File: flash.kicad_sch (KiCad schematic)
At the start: 16 parts, among them J5001 Tag-Connect_TC2050-IDC-NL_2x5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, J5002 Socket_SOP2-16_ACA-SPI-006-K0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, J5003 PinHeader_2x4_P2.54mm_Drill1.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, U5001 MT25QU01GBBB8_SOIC

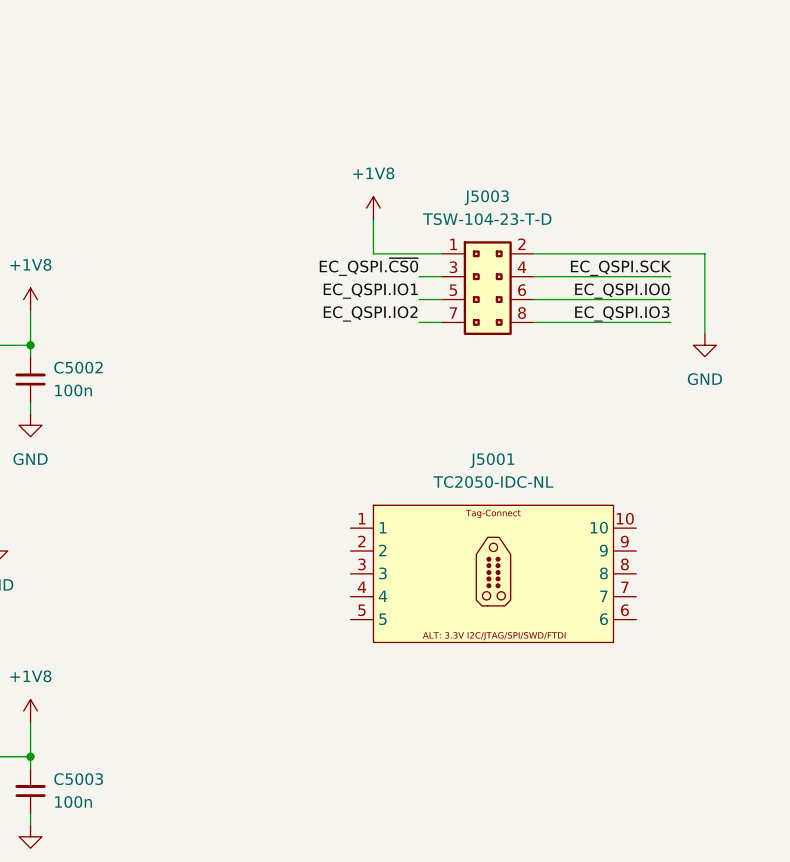
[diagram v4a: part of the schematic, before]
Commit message: [#103224] Add root schematic connections, add EMDRST button, add 1u decoupling capacitors, connect UART, add fiducials
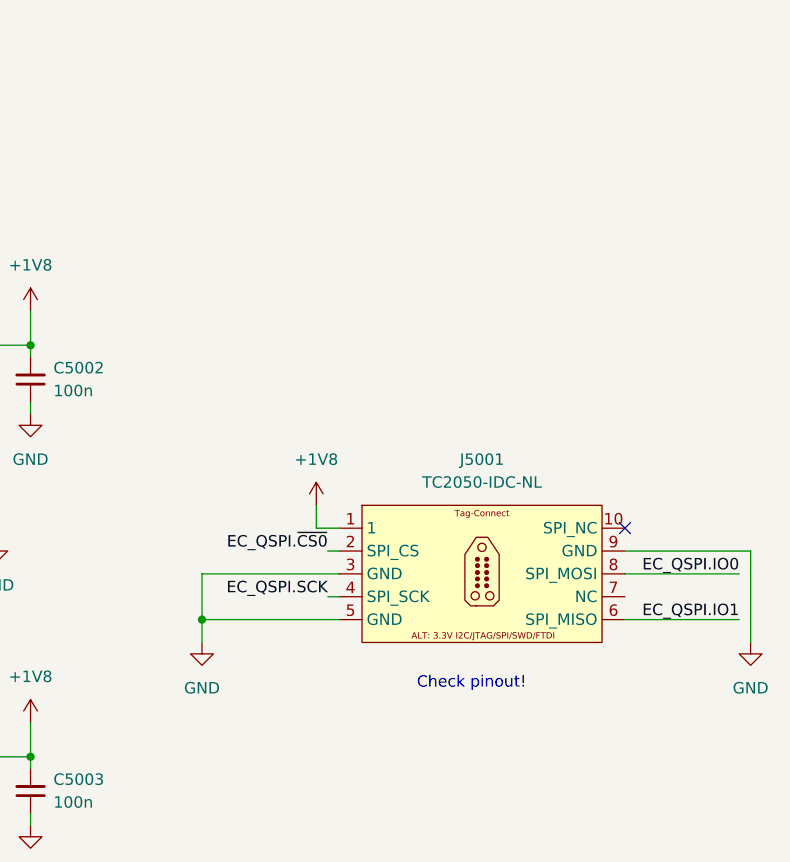
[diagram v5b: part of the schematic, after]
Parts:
- removed J5003: PinHeader_2x4_P2.54mm_Drill1.02mm, antmicro-footprints:PinHeader_2x4_P2.54mm_Drill1.02mm, symbol Antmicro Symbols:PinHeader_2x4_P2.54mm_Drill1.02mm
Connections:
- net +1V8: now also J5001.1
- net EC_QSPI.IO0: now also J5001.8
- net EC_QSPI.IO1: now also J5001.6
- net EC_QSPI.SCK: now also J5001.4
- net EC_QSPI.~{CS0}: now also J5001.2
- net GND: now also J5001.3, J5001.5, J5001.9
- no-connect marks 0 -> 1
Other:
- note added: "Check pinout!"
- moved on the sheet: J5001

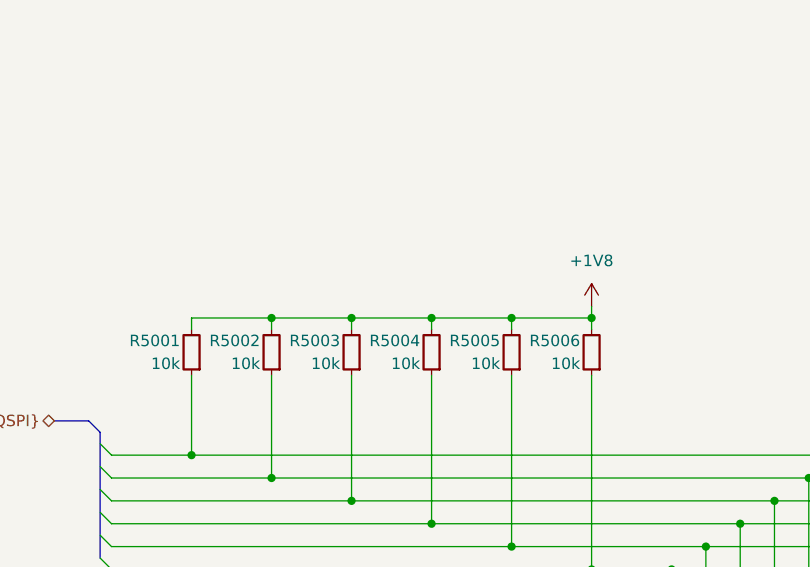
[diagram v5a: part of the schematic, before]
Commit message: [#103224] Add strapping pins, check for signals needed to boot, add breakout connectors, add testpoints
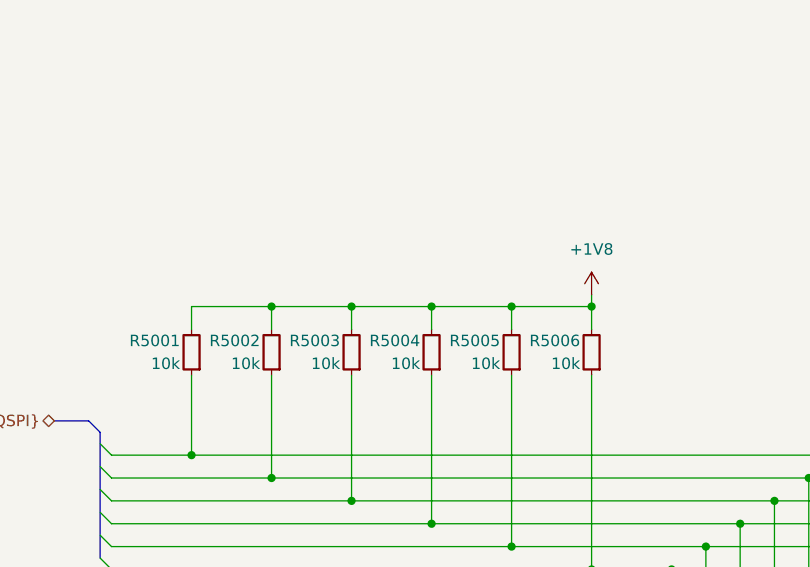
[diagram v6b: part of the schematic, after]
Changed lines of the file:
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@@
 	)
 	(junction
-		(at 87.63 68.58)
+		(at 87.63 67.31)
 		(diameter 0)
 		(color 0 0 0 0)
@@
 	)
 	(junction
-		(at 69.85 68.58)
+		(at 69.85 67.31)
 		(diameter 0)
 		(color 0 0 0 0)
@@
 	)
 	(junction
-		(at 96.52 68.58)
+		(at 96.52 67.31)
 		(diameter 0)
 		(color 0 0 0 0)
@@
 	)
 	(junction
-		(at 105.41 68.58)
+		(at 105.41 67.31)
 		(diameter 0)
 		(color 0 0 0 0)
@@
 	)
 	(junction
-		(at 78.74 68.58)
+		(at 78.74 67.31)
 		(diameter 0)
 		(color 0 0 0 0)
@@
 	(wire
 		(pts
-			(xy 105.41 68.58) (xy 96.52 68.58)
+			(xy 105.41 67.31) (xy 96.52 67.31)
 		)
 		(stroke
@@
 	(wire
 		(pts
-			(xy 69.85 68.58) (xy 69.85 69.85)
+			(xy 69.85 67.31) (xy 69.85 69.85)
 		)
 		(stroke
@@
 	(wire
 		(pts
-			(xy 96.52 68.58) (xy 87.63 68.58)
+			(xy 96.52 67.31) (xy 87.63 67.31)
 		)
 		(stroke
@@
 	(wire
 		(pts
-			(xy 60.96 68.58) (xy 60.96 69.85)
-		)
-		(stroke
-			(width 0)
-			(type default)
-		)
-	)
-	(wire
-		(pts
-			(xy 78.74 68.58) (xy 78.74 69.85)
+			(xy 60.96 67.31) (xy 60.96 69.85)
+		)
+		(stroke
+			(width 0)
+			(type default)
+		)
+	)
+	(wire
+		(pts
+			(xy 78.74 67.31) (xy 78.74 69.85)
 		)
 		(stroke
@@
 	(wire
 		(pts
-			(xy 96.52 68.58) (xy 96.52 69.85)
+			(xy 96.52 67.31) (xy 96.52 69.85)
 		)
 		(stroke
@@
 	(wire
 		(pts
-			(xy 105.41 67.31) (xy 105.41 68.58)
+			(xy 105.41 66.04) (xy 105.41 67.31)
 		)
 		(stroke
@@
 	(wire
 		(pts
-			(xy 78.74 68.58) (xy 69.85 68.58)
+			(xy 78.74 67.31) (xy 69.85 67.31)
 		)
 		(stroke
@@
 	(wire
 		(pts
-			(xy 105.41 69.85) (xy 105.41 68.58)
+			(xy 105.41 69.85) (xy 105.41 67.31)
 		)
 		(stroke
@@
 	(wire
 		(pts
-			(xy 87.63 68.58) (xy 78.74 68.58)
+			(xy 87.63 67.31) (xy 78.74 67.31)
 		)
 		(stroke
@@
 	(wire
 		(pts
-			(xy 69.85 68.58) (xy 60.96 68.58)
+			(xy 69.85 67.31) (xy 60.96 67.31)
 		)
 		(stroke
@@
 	(wire
 		(pts
-			(xy 87.63 68.58) (xy 87.63 69.85)
+			(xy 87.63 67.31) (xy 87.63 69.85)
 		)
 		(stroke
@@
 	(symbol
 		(lib_id "antmicropower:+1V8")
-		(at 105.41 67.31 0)
+		(at 105.41 66.04 0)
 		(unit 1)
 		(body_style 1)
@@
 		(fields_autoplaced yes)
 		(property "Reference" "#PWR05001"
-			(at 120.65 69.85 0)
+			(at 120.65 68.58 0)
 			(hide yes)
 			(show_name no)
@@
 		)
 		(property "Value" "+1V8"
-			(at 105.41 62.23 0)
+			(at 105.41 60.96 0)
 			(show_name no)
 			(do_not_autoplace no)
@@
 		)
 		(property "Footprint" ""
-			(at 120.65 74.93 0)
+			(at 120.65 73.66 0)
 			(hide yes)
 			(show_name no)
@@
 		)
 		(property "Datasheet" ""
-			(at 120.65 77.47 0)
+			(at 120.65 76.2 0)
 			(hide yes)
 			(show_name no)
@@
 		)
 		(property "Description" ""
-			(at 120.65 80.01 0)
+			(at 120.65 78.74 0)
 			(hide yes)
 			(show_name no)
@@
 		)
 		(property "Author" "Antmicro"
-			(at 120.65 72.39 0)
+			(at 120.65 71.12 0)
 			(hide yes)
 			(show_name no)
@@
 		)
 		(property "License" "Apache-2.0"
-			(at 120.65 74.93 0)
-			(hide yes)
-			(show_name no)
+			(at 120.65 73.66 0)
+			(hide yes)
+			(show_name no)

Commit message: [#103224] Add notes to schematic, fix typos, fix gpio connections, bump date
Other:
- note added: "Layout guides are different than eval design - check it"
- note added: "Serial resistors?"
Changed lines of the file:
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@@
 	(generator_version "10.0")
 	(paper "A4")
+	(text "Layout guides are different than eval design - check it"
+		(exclude_from_sim no)
+		(at 78.994 100.584 0)
+		(effects
+			(font
+				(size 1.27 1.27)
+			)
+		)
+	)
+	(text "Serial resistors?"
+		(exclude_from_sim no)
+		(at 59.436 104.14 0)
+		(effects
+			(font
+				(size 1.27 1.27)
+			)
+		)
+	)
 	(text "Check pinout!"
 		(exclude_from_sim no)

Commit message: chore: set date and project name
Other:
- company: (none) -> Antmicro
- title: (none) -> eSPI Adapter
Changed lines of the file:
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@@
 	(generator_version "10.0")
 	(paper "A4")
+	(title_block
+		(title "eSPI Adapter")
+		(date "2026-08-21")
+		(rev "1.0.0")
+		(company "Antmicro")
+	)
 	(text "Layout guides are different than eval design - check it"
 		(exclude_from_sim no)
